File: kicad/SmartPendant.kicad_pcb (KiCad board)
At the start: 2 copper layers, 125 x 59 mm, 51 parts, among them J1 UART, J2 ST-LINK, J3 Encoder, J5 Display, J6 USB_C_Receptacle_USB2.0_16P, J8 Micro_SD_Card_Det1, Q1 MMBT3904, U1 WEACT BLACKPILL F4X1, U2 AMS1117-3.3, U3 MB85RC256VPNF-G-JNERE1

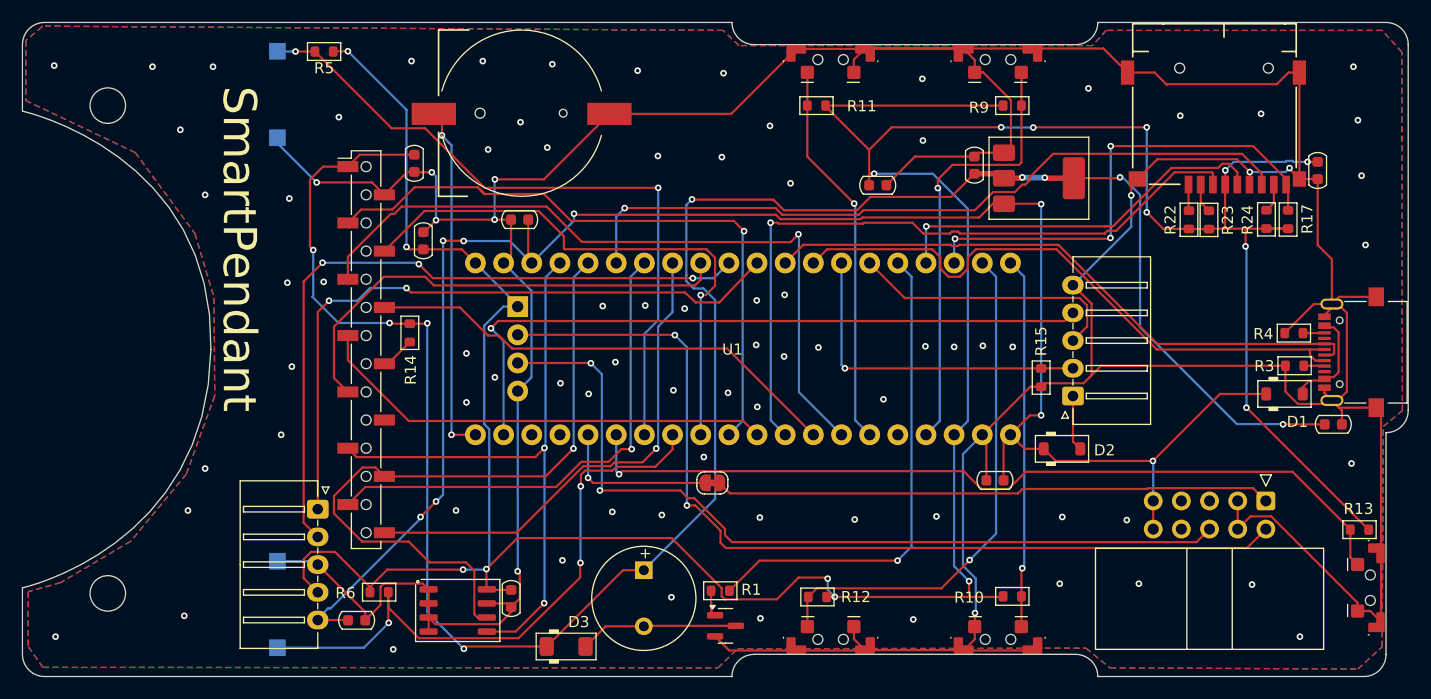
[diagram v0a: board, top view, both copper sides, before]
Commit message: Fix orientation of display connector.
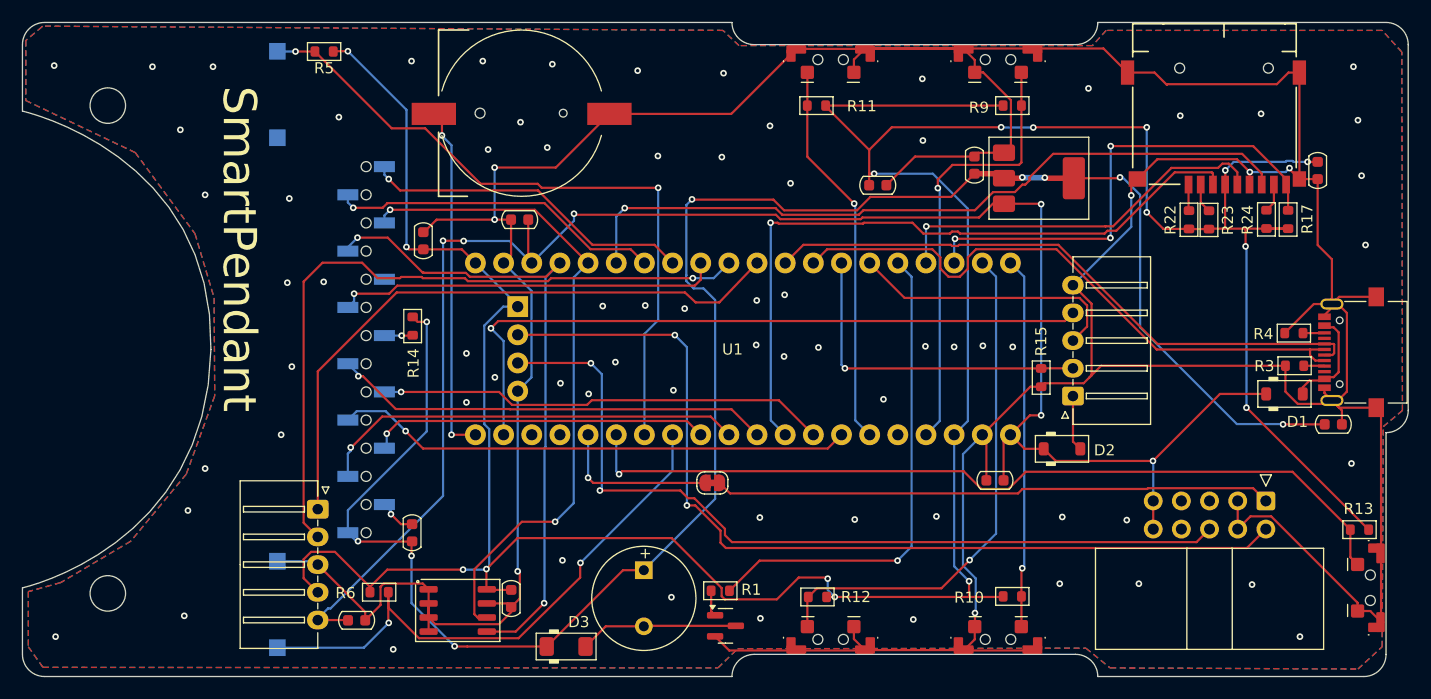
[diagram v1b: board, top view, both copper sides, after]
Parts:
- J5: moved to B.Cu
- moved C8 33.3 mm to (160.1, 94.0), turned to 90 degrees
- moved R14 0.66 mm to (160.2, 75.4)
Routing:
- net +3.3V: track 195.6 -> 173.9 mm
- net LCD_RST: track 50.5 -> 30.7 mm
- net LCD_CS: track 58.1 -> 38.7 mm
- net LCD_DC: track 65.9 -> 46.8 mm
- net GND: track 445.6 -> 428.5 mm, vias 87 -> 79
- net TOUCH_RST: track 45.0 -> 30.0 mm
- net TOUCH_INT: track 45.0 -> 30.1 mm
- net LCD_MISO: track 43.4 -> 34.8 mm, vias 0 -> 1
- net RIGHT_BTN: track 55.7 -> 52.2 mm, vias 3 -> 2
- net ENC_A: track 60.3 -> 56.9 mm, vias 2 -> 0
- net SDA: track 55.9 -> 59.3 mm
- net LCD_MOSI: track 43.4 -> 40.6 mm, vias 0 -> 1
- net SCL: track 62.9 -> 60.2 mm, vias 1 -> 2
- net LCD_SCK: track 41.9 -> 39.7 mm, vias 0 -> 1
- net Net-(J5-Pin_8): track 3.11 -> 2.57 mm, vias 0 -> 1
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
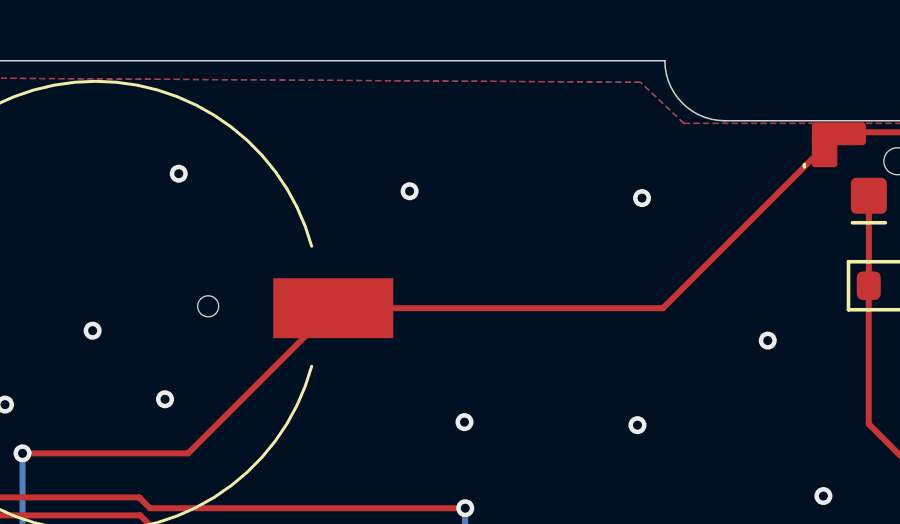
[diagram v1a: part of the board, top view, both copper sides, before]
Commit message: Add GND test point.
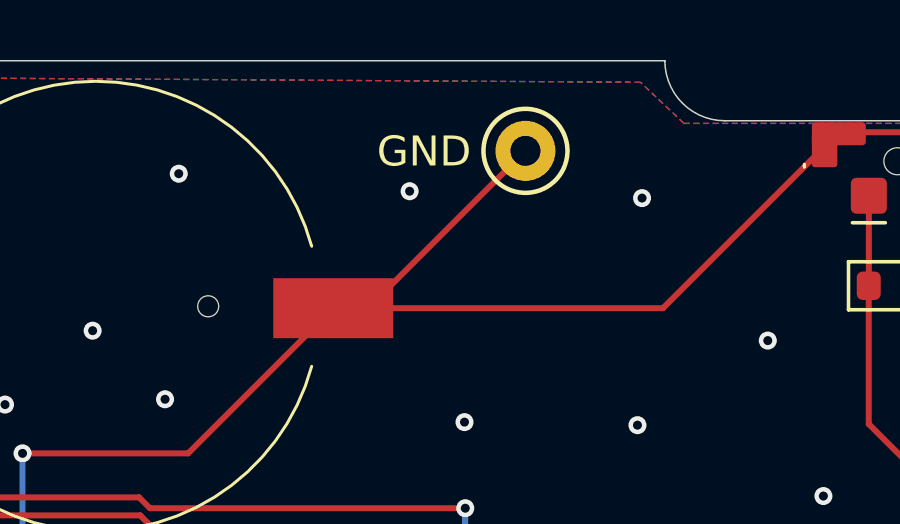
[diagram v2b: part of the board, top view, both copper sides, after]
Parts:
- added TP1: GND, TestPoint:TestPoint_Keystone_5000-5004_Miniature, F.Cu at (184.4, 51.0)
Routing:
- net GND: track 428.5 -> 438.2 mm
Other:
- board text added: "GND"
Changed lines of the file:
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@@
 		)
 	)
+	(footprint "TestPoint:TestPoint_Keystone_5000-5004_Miniature"
+		(layer "F.Cu")
+		(at 184.3532 51.0032)
+		(descr "Keystone Miniature THM Test Point 5000-5004, http://www.keyelco.com/product-pdf.cfm?p=1309")
+		(tags "Through Hole Mount Test Points")
+		(property "Reference" "TP1"
+			(at 0 -2.5 0)
+			(layer "F.SilkS")
+			(hide yes)
+			(effects
+				(font
+					(size 1 1)
+					(thickness 0.15)
+				)
+			)
+		)
+		(property "Value" "GND"
+			(at 0 2.5 0)
+			(layer "F.Fab")
+			(effects
+				(font
+					(size 1 1)
+					(thickness 0.15)
+				)
+			)
+		)
+		(property "Datasheet" "~"
+			(at 0 0 0)
+			(layer "F.Fab")
+			(hide yes)
+			(effects
+				(font
+					(size 1.27 1.27)
+					(thickness 0.15)
+				)
+			)
+		)
+		(property "Description" "test point"
+			(at 0 0 0)
+			(layer "F.Fab")
+			(hide yes)
+			(effects
+				(font
+					(size 1.27 1.27)
+					(thickness 0.15)
+				)
+			)
+		)
+		(property ki_fp_filters "Pin* Test*")
+		(sheetname "/")
+		(sheetfile "SmartPendant.kicad_sch")
+		(attr through_hole)
+		(fp_circle
+			(center 0 0)
+			(end 1.4 0)
+			(stroke
+				(width 0.15)
+				(type solid)
+			)
+			(fill no)
+			(layer "F.SilkS")
+		)
+		(fp_circle
+			(center 0 0)
+			(end 1.65 0)
+			(stroke
+				(width 0.05)
+				(type solid)
+			)
+			(fill no)
+			(layer "F.CrtYd")
+		)
+		(fp_line
+			(start -0.75 -0.25)
+			(end 0.75 -0.25)
+			(stroke
+				(width 0.15)
+				(type solid)
+			)
+			(layer "F.Fab")
+		)
+		(fp_line
+			(start -0.75 0.25)
+			(end -0.75 -0.25)
+			(stroke
+				(width 0.15)
+				(type solid)
+			)
+			(layer "F.Fab")
+		)
+		(fp_line
+			(start 0.75 -0.25)
+			(end 0.75 0.25)
+			(stroke
+				(width 0.15)
+				(type solid)
+			)
+			(layer "F.Fab")
+		)
+		(fp_line
+			(start 0.75 0.25)
+			(end -0.75 0.25)
+			(stroke
+				(width 0.15)
+				(type solid)
+			)
+			(layer "F.Fab")
+		)
+		(fp_circle
+			(center 0 0)
+			(end 1.25 0)
+			(stroke
+				(width 0.15)
+				(type solid)
+			)
+			(fill no)
+			(layer "F.Fab")
+		)
+		(fp_text user "${REFERENCE}"
+			(at 0 -2.5 0)
+			(layer "F.Fab")
+			(effects
+				(font
+					(size 1 1)
+					(thickness 0.15)
+				)
+			)
+		)
+		(pad "1" thru_hole circle
+			(at 0 0)
+			(size 2 2)
+			(drill 1)
+			(layers "*.Cu" "*.Mask")
+			(remove_unused_layers no)
+			(net 1 "GND")
+			(pinfunction "1")
+			(pintype "passive")
+		)
+		(embedded_fonts no)
+		(model "${KICAD6_3DMODEL_DIR}/TestPoint.3dshapes/TestPoint_Keystone_5000-5004_Miniature.wrl"
+			(offset
+				(xyz 0 0 0)
+			)
+			(scale
+				(xyz 1 1 1)
+			)
+			(rotate
+				(xyz 0 0 0)
+			)
+		)
+	)
 	(footprint "PCM_Capacitor_SMD_AKL:C_0603_1608Metric"
 		(layer "F.Cu")
@@
 		(layer "Edge.Cuts")
 	)
+	(gr_text "GND"
+		(at 179.4002 51.6128 0)
+		(layer "F.SilkS")
+		(effects
+			(font
+				(size 1 1)
+				(thickness 0.1)
+			)
+			(justify left bottom)
+		)
+	)
 	(gr_text "SmartPendant"
 		(at 142.7988 53.721 270)
@@
 	)
 	(segment
+		(start 179.1335 56.2483)
+		(end 177.9476 56.2483)
+		(width 0.2)
+		(layer "F.Cu")
+		(net 1)
+	)
+	(segment
 		(start 243.1166 73.4)
 		(end 241.4848 73.4)
@@
 	)
 	(segment
+		(start 179.1081 56.2483)
+		(end 177.9476 56.2483)
+		(width 0.2)
+		(layer "F.Cu")
+		(net 1)
+	)
+	(segment
 		(start 219.7608 71.6972)
 		(end 221.4368 73.3732)
@@
 		(width 0.2)
 		(layer "F.Cu")
+		(net 1)
+	)
+	(segment
+		(start 184.3532 51.0032)
+		(end 179.1081 56.2483)
+		(width 0.2)
+		(layer "F.Cu")

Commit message: Add labels.
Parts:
- moved R15 8.87 mm to (223.4, 86.1), turned to 0 degrees
- moved C2 2.93 mm to (158.1, 102.2)
- moved R6 0.97 mm to (158.1, 99.2)
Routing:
- net GND: track 438.2 -> 415.5 mm
- net UART_RX: track 30.2 -> 38.3 mm
- net VCC: track 305.6 -> 299.0 mm
- net +5V: track 163.2 -> 166.2 mm
- net RIGHT_BTN: track 52.2 -> 51.3 mm
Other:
- board text added: "3V3"
- board text added: "5V"
- board text added: "A"
- board text added: "B"
- board text added: "EN"
- board text added: "RESET"
- board text added: "RX"
- board text added: "TX"

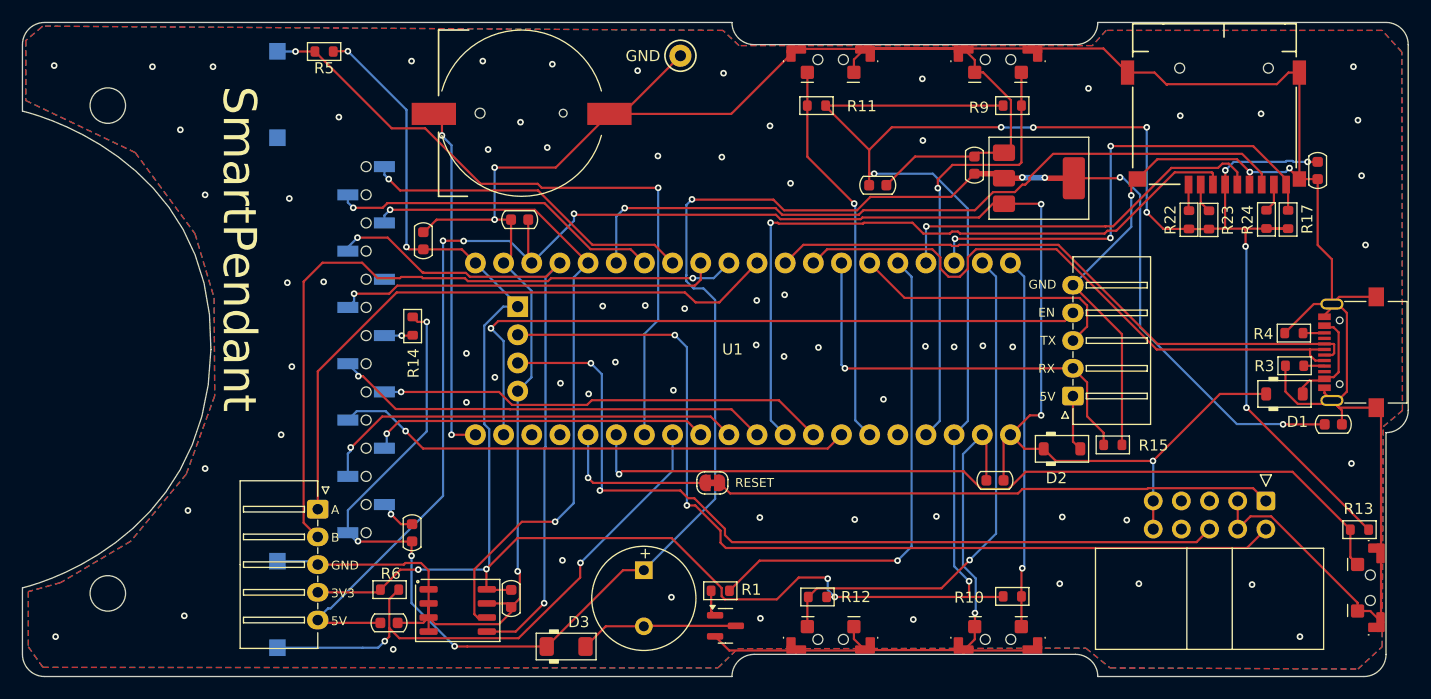
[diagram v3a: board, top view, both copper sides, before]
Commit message: Invert A, B.
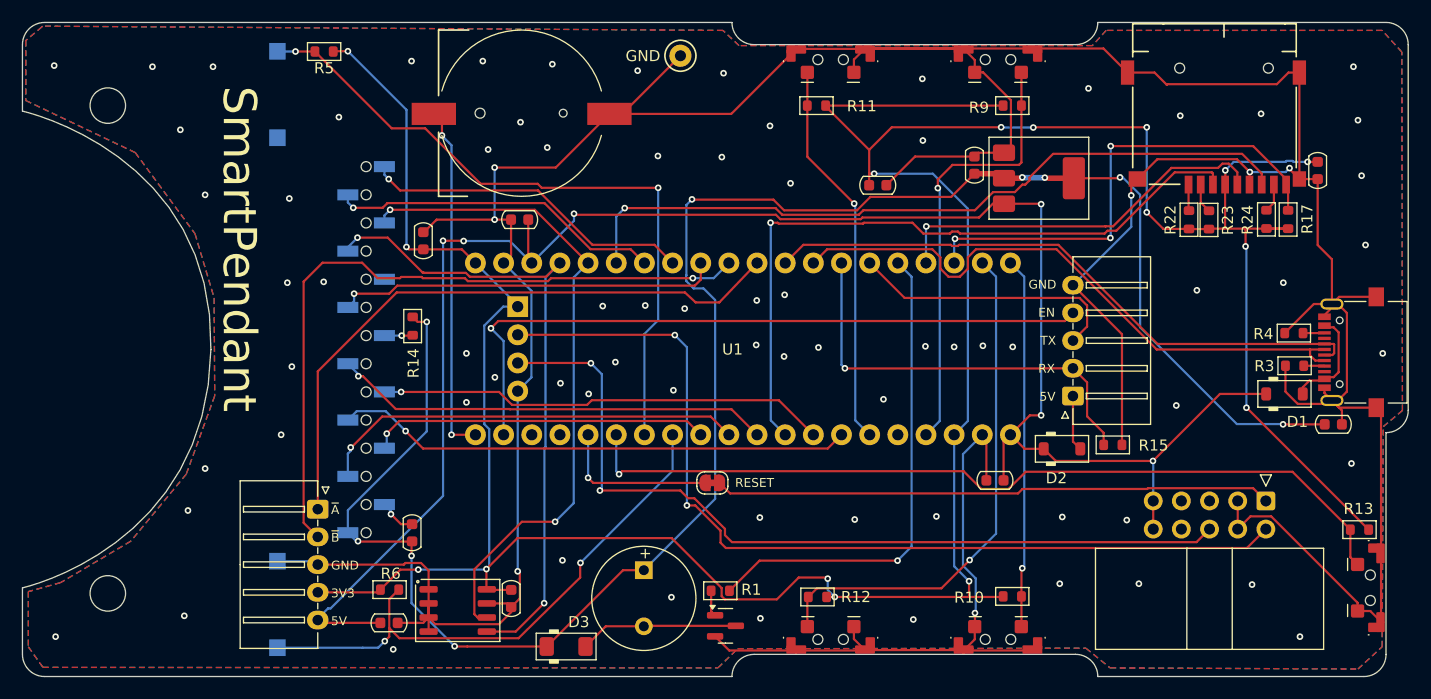
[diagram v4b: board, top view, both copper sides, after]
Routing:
- net GND: vias 79 -> 83
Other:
- board text added: "~{A}"
- board text added: "~{B}"
- board text removed: "A"
- board text removed: "B"
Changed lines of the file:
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@@
 		)
 	)
-	(gr_text "A"
+	(gr_text "~{A}"
 		(at 152.8318 92.4306 0)
 		(layer "F.SilkS")
@@
 		)
 	)
-	(gr_text "B"
+	(gr_text "~{B}"
 		(at 152.8318 94.93885 0)
 		(layer "F.SilkS")
@@
 	)
 	(via
+		(at 229.0826 82.55)
+		(size 0.6)
+		(drill 0.3)
+		(layers "F.Cu" "B.Cu")
+		(free yes)
+		(net 1)
+	)
+	(via
 		(at 193.7512 72.5678)
 		(size 0.6)
@@
 	)
 	(via
+		(at 238.7346 71.4756)
+		(size 0.6)
+		(drill 0.3)
+		(layers "F.Cu" "B.Cu")
+		(free yes)
+		(net 1)
+	)
+	(via
 		(at 200.0758 92.837)
 		(size 0.6)
@@
 	)
 	(via
+		(at 230.9368 72.1614)
+		(size 0.6)
+		(drill 0.3)
+		(layers "F.Cu" "B.Cu")
+		(free yes)
+		(net 1)
+	)
+	(via
 		(at 172.339 59.2836)
 		(size 0.6)
@@
 		(size 0.6)
 		(drill 0.3)
+		(layers "F.Cu" "B.Cu")
+		(free yes)
+		(net 1)
+	)
+	(via
+		(at 247.7008 77.851)
+		(size 0.6)
+		(drill 0.3)

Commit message: Use resistor array; make references consecutive.
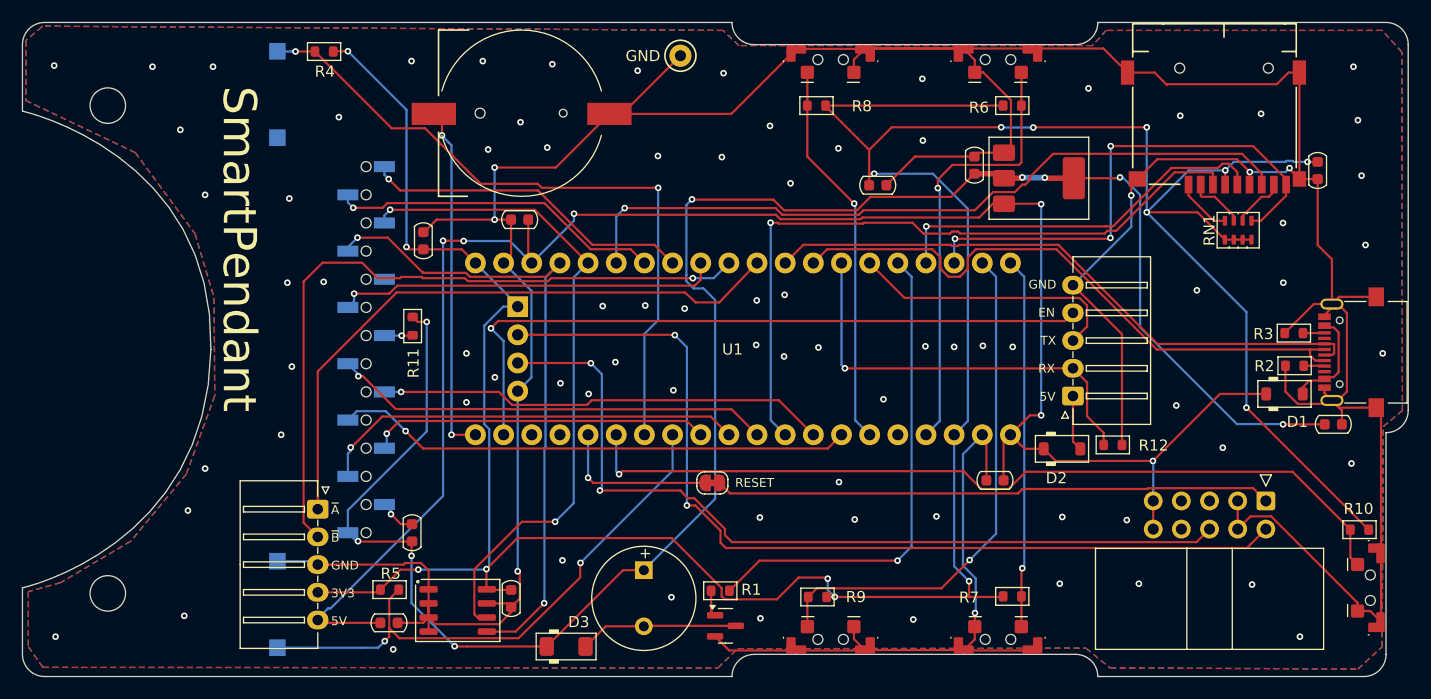
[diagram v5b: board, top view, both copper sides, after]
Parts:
- removed R17: 1k, PCM_Resistor_SMD_AKL:R_0603_1608Metric
- removed R22, R23, R24: 10k, PCM_Resistor_SMD_AKL:R_0603_1608Metric
- added RN1: 10k, PCM_Resistor_SMD_AKL:R_Array_Concave_4x0603, F.Cu at (234.7, 66.7)
- renumbered J5 to J4, J6 to J5, J8 to J6, R13 to R10, R14 to R11, R15 to R12, R3 to R2, R4 to R3, R5 to R4, R6 to R5, R9 to R6, R10 to R7, R11 to R8, R12 to R9
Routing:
- net VCC: track 299.0 -> 304.0 mm, vias 16 -> 15
- net SDIO_CD: track 44.5 -> 47.4 mm
- net Net-(J6-DAT2): track 2.37 -> 5.22 mm
- net Net-(J6-DAT3/CD): track 2.67 -> 5.18 mm
- net Net-(J6-DAT1): track 2.59 -> 4.82 mm
- net GND: vias 83 -> 87

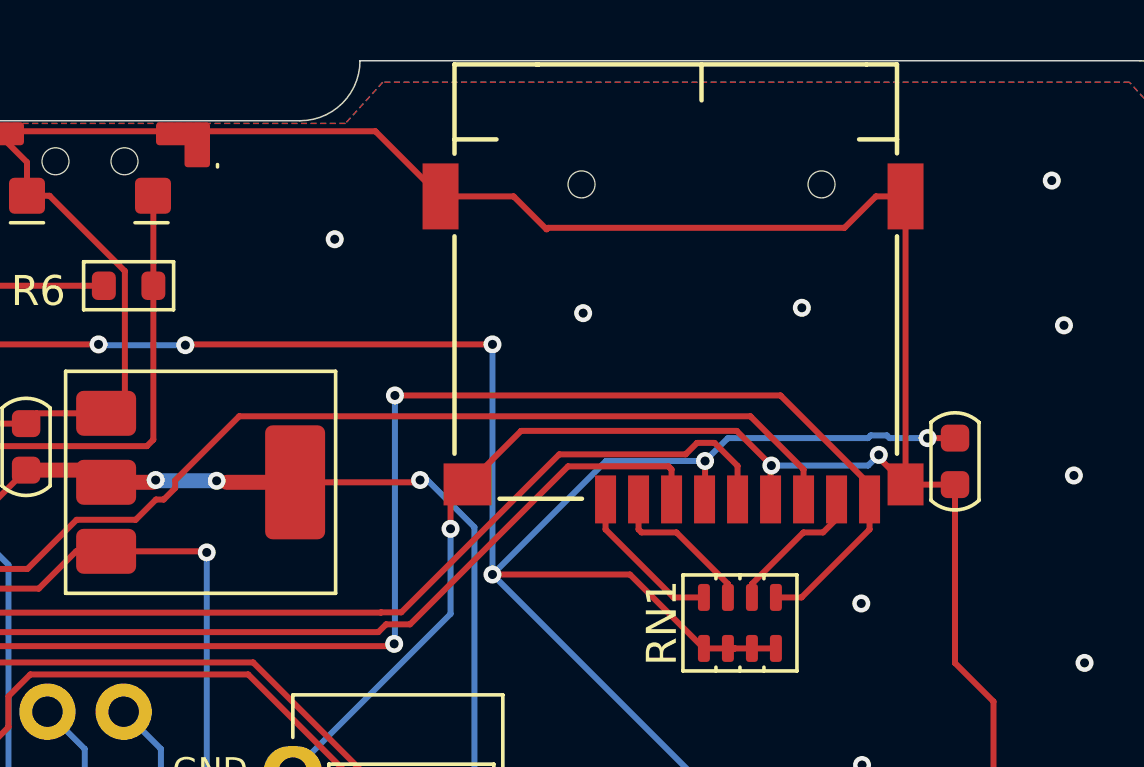
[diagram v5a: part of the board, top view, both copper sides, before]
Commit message: Optimize SD card footprint and routing.
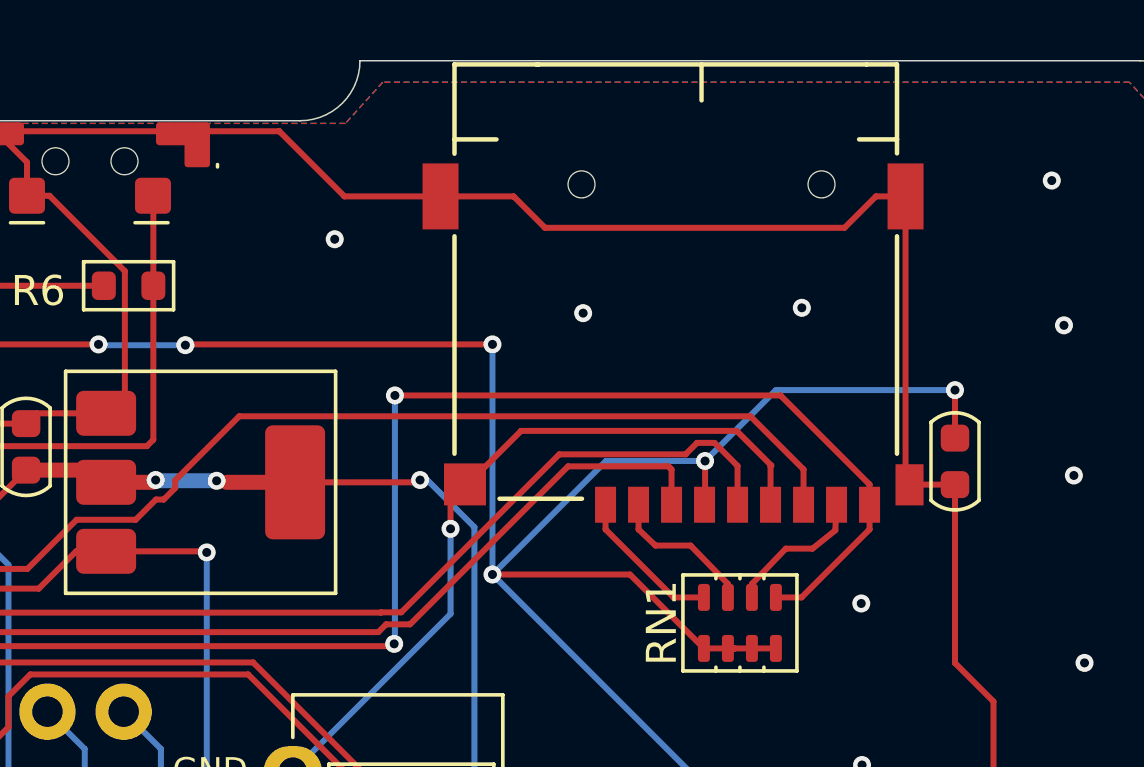
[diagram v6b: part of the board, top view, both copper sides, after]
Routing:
- net GND: track 415.5 -> 410.3 mm, vias 87 -> 85
- net VCC: track 304.0 -> 306.2 mm
